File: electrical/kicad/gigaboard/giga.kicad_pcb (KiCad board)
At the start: 2 copper layers, 88.3 x 54 mm, 2 parts

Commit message: update(giga): pcb layout #01
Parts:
- removed ?: , clipboard:050be39d-fed9-491a-89e1-a26c1a1eb318
- added F1: F_Small, Fuse_TE5_Littlefuse-395Series, F.Cu at (120.0, 89.9)
- added REF**: PinHeader_1x04_P2.54mm_Vertical, Connector_PinHeader_2.54mm:PinHeader_1x04_P2.54mm_Vertical, F.Cu at (181.0, 58.1)
- added REF**: MKS_TMC2209, Motor_Driver:MKS_TMC2209, F.Cu at (151.0, 61.9)
- added REF**: JST_EH_B4B-EH-A_1x04_P2.50mm_Vertical, Connector_JST:JST_EH_B4B-EH-A_1x04_P2.50mm_Vertical, F.Cu at (207.0, 59.2)
- added REF**: TerminalBlock_Phoenix_MKDS-1,5-3-5.08_1x03_P5.08mm_Horizont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, TerminalBlock_Phoenix:TerminalBlock_Phoenix_MKDS-1,5-3-5.08_1x03_P5.08mm_Horizontal, F.Cu at (112.0, 91.0)
- added REF**: MKS_TMC2209, Motor_Driver:MKS_TMC2209, F.Cu at (170.7, 61.0)
- added REF**: MKS_TMC2209, Motor_Driver:MKS_TMC2209, F.Cu at (151.0, 83.0)
- added REF**: PinHeader_1x04_P2.54mm_Vertical, Connector_PinHeader_2.54mm:PinHeader_1x04_P2.54mm_Vertical, F.Cu at (140.0, 58.1)
- added REF**: PinHeader_2x10_P2.54mm_Vertical, Connector_PinHeader_2.54mm:PinHeader_2x10_P2.54mm_Vertical, F.Cu at (188.0, 54.3)
- added REF**: PinHeader_1x04_P2.54mm_Vertical, Connector_PinHeader_2.54mm:PinHeader_1x04_P2.54mm_Vertical, F.Cu at (140.0, 79.2)
- added REF**: JST_EH_B4B-EH-A_1x04_P2.50mm_Vertical, Connector_JST:JST_EH_B4B-EH-A_1x04_P2.50mm_Vertical, F.Cu at (189.5, 89.0)
- added REF**: JST_EH_B4B-EH-A_1x04_P2.50mm_Vertical, Connector_JST:JST_EH_B4B-EH-A_1x04_P2.50mm_Vertical, F.Cu at (201.5, 87.5)
- added REF**: MKS_TMC2209, Motor_Driver:MKS_TMC2209, F.Cu at (130.3, 82.9)
- added REF**: JST_EH_B4B-EH-A_1x04_P2.50mm_Vertical, Connector_JST:JST_EH_B4B-EH-A_1x04_P2.50mm_Vertical, F.Cu at (119.2, 62.2)
- added REF**: JST_EH_B4B-EH-A_1x04_P2.50mm_Vertical, Connector_JST:JST_EH_B4B-EH-A_1x04_P2.50mm_Vertical, F.Cu at (189.5, 94.0)
- added REF**: PinHeader_1x04_P2.54mm_Vertical, Connector_PinHeader_2.54mm:PinHeader_1x04_P2.54mm_Vertical, F.Cu at (160.7, 58.1)
- added REF**: MKS_TMC2209, Motor_Driver:MKS_TMC2209, F.Cu at (170.8, 82.0)
- added REF**: PinHeader_1x04_P2.54mm_Vertical, Connector_PinHeader_2.54mm:PinHeader_1x04_P2.54mm_Vertical, F.Cu at (160.7, 79.3)
- added REF**: JST_EH_B4B-EH-A_1x04_P2.50mm_Vertical, Connector_JST:JST_EH_B4B-EH-A_1x04_P2.50mm_Vertical, F.Cu at (206.9, 73.5)
- added REF**: JST_EH_B4B-EH-A_1x04_P2.50mm_Vertical, Connector_JST:JST_EH_B4B-EH-A_1x04_P2.50mm_Vertical, F.Cu at (206.9, 87.5)
- added REF**: JST_EH_B4B-EH-A_1x04_P2.50mm_Vertical, Connector_JST:JST_EH_B4B-EH-A_1x04_P2.50mm_Vertical, F.Cu at (201.5, 73.5)
- added REF**: MKS_TMC2209, Motor_Driver:MKS_TMC2209, F.Cu at (130.3, 61.9)
- added REF**: JST_EH_B4B-EH-A_1x04_P2.50mm_Vertical, Connector_JST:JST_EH_B4B-EH-A_1x04_P2.50mm_Vertical, F.Cu at (201.6, 59.2)
- added REF**: PinHeader_1x04_P2.54mm_Vertical, Connector_PinHeader_2.54mm:PinHeader_1x04_P2.54mm_Vertical, F.Cu at (167.2, 94.5)
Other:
- board size 88.3 x 54 mm -> 106.5 x 56 mm

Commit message: update(giga): pcb layout #02
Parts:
- removed REF** (x6): PinHeader_1x04_P2.54mm_Vertical, Connector_PinHeader_2.54mm:PinHeader_1x04_P2.54mm_Vertical
- removed REF** (x6): MKS_TMC2209, Motor_Driver:MKS_TMC2209
- removed REF** (x9): JST_EH_B4B-EH-A_1x04_P2.50mm_Vertical, Connector_JST:JST_EH_B4B-EH-A_1x04_P2.50mm_Vertical
- removed REF**: TerminalBlock_Phoenix_MKDS-1,5-3-5.08_1x03_P5.08mm_Horizont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, TerminalBlock_Phoenix:TerminalBlock_Phoenix_MKDS-1,5-3-5.08_1x03_P5.08mm_Horizontal
- removed REF**: PinHeader_2x10_P2.54mm_Vertical, Connector_PinHeader_2.54mm:PinHeader_2x10_P2.54mm_Vertical
- added C1: 100uF, Capacitor_SMD:CP_Elec_6.3x7.7, F.Cu at (107.4, 48.3)
- added C2: 100uF, Capacitor_SMD:CP_Elec_6.3x7.7, F.Cu at (107.4, 68.6)
- added C3: 100uF, Capacitor_SMD:CP_Elec_6.3x7.7, F.Cu at (127.8, 48.3)
- added C4: 100uF, Capacitor_SMD:CP_Elec_6.3x7.7, F.Cu at (127.8, 68.6)
- added C5: 100uF, Capacitor_SMD:CP_Elec_6.3x7.7, F.Cu at (148.1, 48.3)
- added C6: 100uF, Capacitor_SMD:CP_Elec_6.3x7.7, F.Cu at (148.1, 68.6)
- added D1: D, Diode_THT:D_DO-35_SOD27_P7.62mm_Horizontal, F.Cu at (97.8, 81.8)
- added J1: Conn_02x03_Counter_Clockwise, Connector_PinHeader_2.54mm:PinHeader_2x03_P2.54mm_Vertical, F.Cu at (104.9, 59.7)
- added J10: Conn_01x04, Connector_PinHeader_2.54mm:PinHeader_1x04_P2.54mm_Vertical, F.Cu at (137.9, 68.6)
- added J11: Conn_01x04, Connector_PinHeader_2.54mm:PinHeader_1x04_P2.54mm_Vertical, F.Cu at (158.8, 48.3)
- added J12: Conn_01x04, Connector_PinHeader_2.54mm:PinHeader_1x04_P2.54mm_Vertical, F.Cu at (158.8, 75.0)
- added J13: Conn_01x04, Connector_PinHeader_2.54mm:PinHeader_1x04_P2.54mm_Vertical, F.Cu at (176.5, 40.6)
- added J14: Conn_01x04, Connector_PinHeader_2.54mm:PinHeader_1x04_P2.54mm_Vertical, F.Cu at (176.5, 53.3)
- added J15: Conn_01x04, Connector_PinHeader_2.54mm:PinHeader_1x04_P2.54mm_Vertical, F.Cu at (176.5, 66.0)
- added J16: Conn_01x04, Connector_PinHeader_2.54mm:PinHeader_1x04_P2.54mm_Vertical, F.Cu at (180.3, 40.6)
- added J17: Conn_01x04, Connector_PinHeader_2.54mm:PinHeader_1x04_P2.54mm_Vertical, F.Cu at (180.3, 53.3)
- added J18: Conn_01x04, Connector_PinHeader_2.54mm:PinHeader_1x04_P2.54mm_Vertical, F.Cu at (180.3, 66.0)
- added J19: Conn_01x04, Connector_PinHeader_2.54mm:PinHeader_1x04_P2.54mm_Vertical, F.Cu at (96.5, 43.2)
- added J2: Conn_02x04_Counter_Clockwise, Connector_PinHeader_2.54mm:PinHeader_2x03_P2.54mm_Vertical, F.Cu at (104.9, 80.0)
- added J20: Conn_01x04, Connector_PinHeader_2.54mm:PinHeader_1x04_P2.54mm_Vertical, F.Cu at (162.6, 75.0)
- added J21: Conn_01x04, Connector_PinHeader_2.54mm:PinHeader_1x04_P2.54mm_Vertical, F.Cu at (166.4, 75.0)
- added J22: Screw_Terminal_01x03, Connector_Phoenix_MSTB:PhoenixContact_MSTBA_2,5_3-G-5,08_1x03_P5.08mm_Horizontal, F.Cu at (90.1, 60.7)
- added J23: Conn_02x12_Counter_Clockwise, Connector_PinHeader_2.54mm:PinHeader_2x12_P2.54mm_Vertical, F.Cu at (163.8, 43.2)
- added J3: Conn_02x04_Counter_Clockwise, Connector_PinHeader_2.54mm:PinHeader_2x03_P2.54mm_Vertical, F.Cu at (125.2, 59.7)
- added J4: Conn_02x04_Counter_Clockwise, Connector_PinHeader_2.54mm:PinHeader_2x03_P2.54mm_Vertical, F.Cu at (125.2, 80.0)
- added J5: Conn_02x04_Counter_Clockwise, Connector_PinHeader_2.54mm:PinHeader_2x03_P2.54mm_Vertical, F.Cu at (145.5, 59.7)
- added J6: Conn_02x04_Counter_Clockwise, Connector_PinHeader_2.54mm:PinHeader_2x03_P2.54mm_Vertical, F.Cu at (145.5, 80.0)
- added J7: Conn_01x04, Connector_PinHeader_2.54mm:PinHeader_1x04_P2.54mm_Vertical, F.Cu at (117.6, 48.3)
- added J8: Conn_01x04, Connector_PinHeader_2.54mm:PinHeader_1x04_P2.54mm_Vertical, F.Cu at (117.6, 68.6)
- added J9: Conn_01x04, Connector_PinHeader_2.54mm:PinHeader_1x04_P2.54mm_Vertical, F.Cu at (137.9, 48.3)
- added R1: 100k, Resistor_SMD:R_1206_3216Metric_Pad1.30x1.75mm_HandSolder, F.Cu at (104.9, 53.3)
- added R10: 10k, Resistor_SMD:R_1206_3216Metric_Pad1.30x1.75mm_HandSolder, F.Cu at (130.3, 73.7)
- added R11: 10k, Resistor_SMD:R_1206_3216Metric_Pad1.30x1.75mm_HandSolder, F.Cu at (150.6, 53.3)
- added R12: 10k, Resistor_SMD:R_1206_3216Metric_Pad1.30x1.75mm_HandSolder, F.Cu at (150.6, 73.7)
- added R2: 100k, Resistor_SMD:R_1206_3216Metric_Pad1.30x1.75mm_HandSolder, F.Cu at (104.9, 73.7)
- added R3: 100k, Resistor_SMD:R_1206_3216Metric_Pad1.30x1.75mm_HandSolder, F.Cu at (125.2, 53.3)
- added R4: 100k, Resistor_SMD:R_1206_3216Metric_Pad1.30x1.75mm_HandSolder, F.Cu at (125.2, 73.7)
- added R5: 100k, Resistor_SMD:R_1206_3216Metric_Pad1.30x1.75mm_HandSolder, F.Cu at (145.5, 53.3)
- added R6: 100k, Resistor_SMD:R_1206_3216Metric_Pad1.30x1.75mm_HandSolder, F.Cu at (145.5, 73.7)
- added R7: 10k, Resistor_SMD:R_1206_3216Metric_Pad1.30x1.75mm_HandSolder, F.Cu at (110.0, 53.3)
- added R8: 10k, Resistor_SMD:R_1206_3216Metric_Pad1.30x1.75mm_HandSolder, F.Cu at (110.0, 73.7)
- added R9: 10k, Resistor_SMD:R_1206_3216Metric_Pad1.30x1.75mm_HandSolder, F.Cu at (130.3, 53.3)
- added U1: TMC2209, Motor_Driver:MKS_TMC2209, F.Cu at (107.4, 52.1)
- added U2: TMC2209, Motor_Driver:MKS_TMC2209, F.Cu at (107.4, 72.4)
- added U3: TMC2209, Motor_Driver:MKS_TMC2209, F.Cu at (127.8, 52.1)
- added U4: TMC2209, Motor_Driver:MKS_TMC2209, F.Cu at (127.8, 72.4)
- added U5: TMC2209, Motor_Driver:MKS_TMC2209, F.Cu at (148.1, 52.1)
- added U6: TMC2209, Motor_Driver:MKS_TMC2209, F.Cu at (148.1, 72.4)
- F1: footprint Fuse_TE5_Littlefuse-395Series -> Fuse:Fuseholder_Blade_Mini_Keystone_3568
- moved F1 39.3 mm to (82.8, 77.4), turned to 0 degrees
- moved A1 26.3 mm to (76.2, 88.9)
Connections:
- A1 pad AREF: /BAT_MAX -> /+3.3V
- A1 pad D22: /TCA_RST -> /ESTOP
- A1 pad D54: (no net) -> unconnected-(A1-PadD54)
- A1 pad D55: (no net) -> unconnected-(A1-PadD55)
- A1 pad D56: (no net) -> unconnected-(A1-PadD56)
- A1 pad D57: (no net) -> unconnected-(A1-PadD57)
- A1 pad D58: (no net) -> unconnected-(A1-PadD58)
- A1 pad D59: (no net) -> unconnected-(A1-PadD59)
- A1 pad D60: (no net) -> unconnected-(A1-PadD60)
- A1 pad D61: (no net) -> unconnected-(A1-PadD61)
- A1 pad D62: (no net) -> unconnected-(A1-PadD62)
- A1 pad D63: (no net) -> unconnected-(A1-PadD63)
- A1 pad D64: (no net) -> unconnected-(A1-PadD64)
- A1 pad D65: (no net) -> unconnected-(A1-PadD65)
- A1 pad D66: (no net) -> unconnected-(A1-PadD66)
- A1 pad D67: (no net) -> unconnected-(A1-PadD67)
- A1 pad D68: (no net) -> unconnected-(A1-PadD68)
- A1 pad D69: (no net) -> unconnected-(A1-PadD69)
- A1 pad D70: (no net) -> unconnected-(A1-PadD70)
- A1 pad D71: (no net) -> unconnected-(A1-PadD71)
- A1 pad D72: (no net) -> unconnected-(A1-PadD72)
- A1 pad D73: (no net) -> unconnected-(A1-PadD73)
- A1 pad D74: (no net) -> unconnected-(A1-PadD74)
- A1 pad D75: (no net) -> unconnected-(A1-PadD75)
- F1 pad 1: (no net) -> /VM
- F1 pad 2: (no net) -> Net-(D1-K)
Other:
- board size 106.5 x 56 mm -> 108 x 66 mm

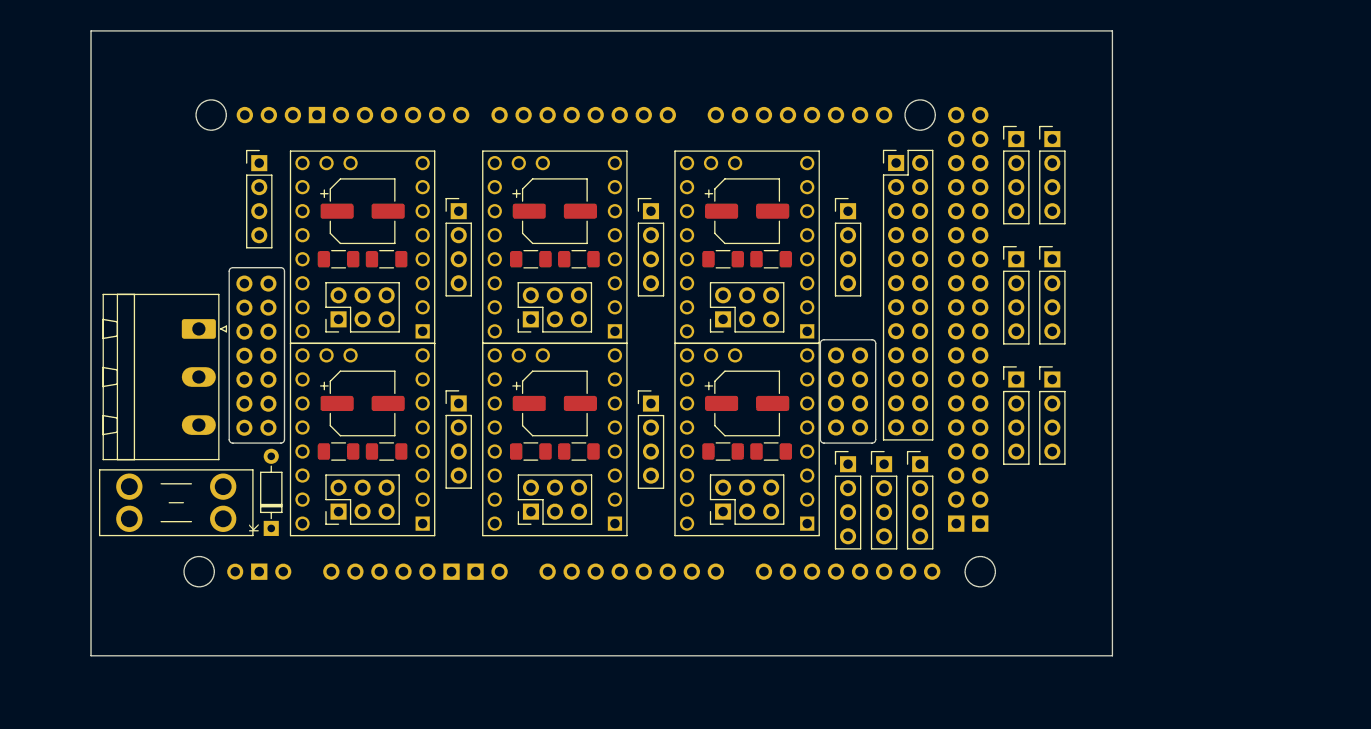
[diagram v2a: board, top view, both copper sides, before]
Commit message: update(giga): pcb wiring complete (DRC passed)
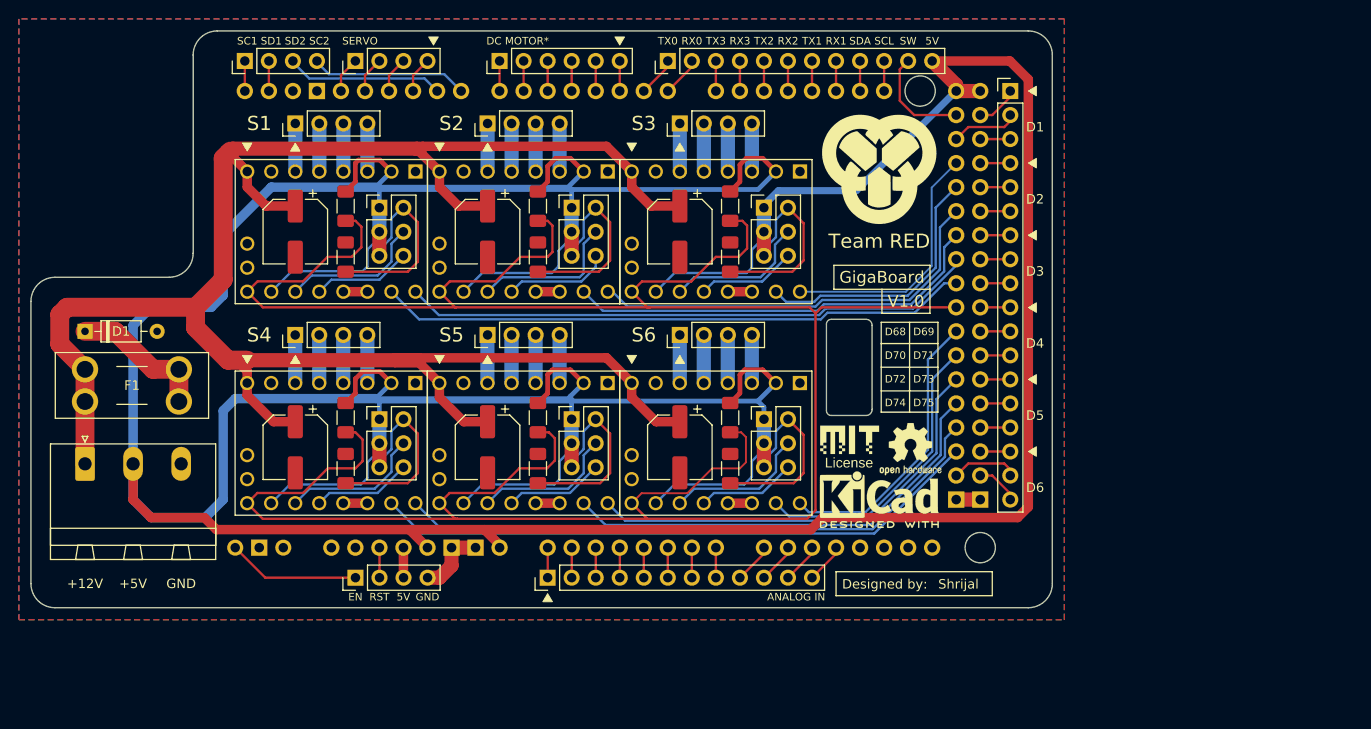
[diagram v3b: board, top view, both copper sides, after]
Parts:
- removed J21: Conn_01x04, Connector_PinHeader_2.54mm:PinHeader_1x04_P2.54mm_Vertical
- removed J22: Screw_Terminal_01x03, Connector_Phoenix_MSTB:PhoenixContact_MSTBA_2,5_3-G-5,08_1x03_P5.08mm_Horizontal
- removed J23: Conn_02x12_Counter_Clockwise, Connector_PinHeader_2.54mm:PinHeader_2x12_P2.54mm_Vertical
- added G***: LOGO, LOGO, F.Cu at (158.9, 73.2)
- added G***: LOGO, LOGO, F.Cu at (161.9, 43.8)
- added REF**: OSHW-Logo2_7.3x6mm_SilkScreen, Symbol:OSHW-Logo2_7.3x6mm_SilkScreen, F.Cu at (165.4, 73.4)
- added REF**: KiCad-Logo2_5mm_SilkScreen, Symbol:KiCad-Logo2_5mm_SilkScreen, F.Cu at (162.1, 78.7)
- J13: value Conn_01x04 -> Conn_01x06; footprint Connector_PinHeader_2.54mm:PinHeader_1x04_P2.54mm_Vertical -> Connector_PinHeader_2.54mm:PinHeader_1x06_P2.54mm_Vertical
- J14: value Conn_01x04 -> Conn_01x18; footprint Connector_PinHeader_2.54mm:PinHeader_1x04_P2.54mm_Vertical -> Connector_PinHeader_2.54mm:PinHeader_1x18_P2.54mm_Vertical
- J16, J18: value Conn_01x04 -> Conn_01x12; footprint Connector_PinHeader_2.54mm:PinHeader_1x04_P2.54mm_Vertical -> Connector_PinHeader_2.54mm:PinHeader_1x12_P2.54mm_Vertical
- J20: value Conn_01x04 -> Screw_Terminal_01x03; footprint Connector_PinHeader_2.54mm:PinHeader_1x04_P2.54mm_Vertical -> Connector_Phoenix_MSTB:PhoenixContact_MSTBA_2,5_3-G-5,08_1x03_P5.08mm_Horizontal
- moved J17 87.9 mm to (95.0, 32.4), turned to 90 degrees
- moved J20 84.5 mm to (78.1, 75.0)
- moved J15 77.5 mm to (106.7, 32.4), turned to 90 degrees
- moved J16 70.7 mm to (127.0, 87.0), turned to 90 degrees
- moved J13 55.2 mm to (121.9, 32.4), turned to 90 degrees
- moved J18 52.8 mm to (139.7, 32.4), turned to 90 degrees
- moved J19 45.0 mm to (106.7, 87.0), turned to 90 degrees
- moved J2 40.5 mm to (129.5, 47.9), turned to 0 degrees
- moved J11 40.3 mm to (120.7, 61.3), turned to 90 degrees
- moved J10 38.3 mm to (100.3, 61.3), turned to 90 degrees
- moved C5 37.1 mm to (120.7, 73.2), turned to -90 degrees
- moved U5 31.4 mm to (124.5, 72.8), turned to -90 degrees
- moved R8 30.5 mm to (126.0, 47.7), turned to -90 degrees
- moved R11 29.8 mm to (126.0, 70.1), turned to -90 degrees
- moved J8 29.7 mm to (120.7, 39.0), turned to 90 degrees
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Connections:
- A1 pad AREF: /+3.3V -> unconnected-(A1-PadAREF)
- A1 pad D26: /DC2_DIR -> /ST3_DIR
- A1 pad D27: /DC2_CHA -> /DC2_DIR
- A1 pad D28: /DC2_CHB -> /ST3_STP
- A1 pad D29: /DC3_DIR -> /DC2_CHA
- A1 pad D30: /DC3_CHA -> /ST2_DIR
- A1 pad D31: /DC3_CHB -> /DC2_CHB
- A1 pad D32: /DC4_DIR -> /ST2_STP
- A1 pad D33: /DC4_CHA -> /DC3_DIR
- A1 pad D34: /DC4_CHB -> /ST1_DIR
- A1 pad D35: /DC5_DIR -> /DC3_CHA
- A1 pad D36: /DC5_CHA -> /ST1_STP
- A1 pad D37: /DC5_CHB -> /DC3_CHB
- A1 pad D38: /DC6_DIR -> /STP_ENA
- A1 pad D39: /DC6_CHA -> /DC4_DIR
- A1 pad D40: /DC6_CHB -> /ST6_DIR
- A1 pad D41: /STP_ENA -> /DC4_CHA
- A1 pad D42: /ST1_STP -> /ST6_STP
- A1 pad D43: /ST1_DIR -> /DC4_CHB
- A1 pad D44: /ST2_STP -> /ST5_DIR
- A1 pad D45: /ST2_DIR -> /DC5_DIR
- A1 pad D46: /ST3_STP -> /ST5_STP
- A1 pad D47: /ST3_DIR -> /DC5_CHA
- A1 pad D48: /ST4_STP -> /ST4_DIR
- A1 pad D49: /ST4_DIR -> /DC5_CHB
- A1 pad D50: /ST5_STP -> /ST4_STP
- A1 pad D51: /ST5_DIR -> /DC6_DIR
- A1 pad D52: /ST6_STP -> /DC6_CHA
- A1 pad D53: /ST6_DIR -> /DC6_CHB
- J13 pad 1: /DC1_PWM -> /DC6_PWM
- J13 pad 2: /DC1_DIR -> /DC5_PWM
- J13 pad 3: /DC1_CHA -> /DC4_PWM
- J13 pad 4: /DC1_CHB -> /DC3_PWM
- J14 pad 1: /DC2_PWM -> /DC1_DIR
- J14 pad 2: /DC2_DIR -> /DC1_CHA
- J14 pad 3: /DC2_CHA -> /DC1_CHB
- J14 pad 4: /DC2_CHB -> /DC2_DIR
- J15 pad 1: /DC3_PWM -> /SV4_PWM
- J15 pad 2: /DC3_DIR -> /SV3_PWM
- J15 pad 3: /DC3_CHA -> /SV2_PWM
- J15 pad 4: /DC3_CHB -> /SV1_PWM
- J16 pad 1: /DC4_PWM -> /BAT1_S1
- J16 pad 2: /DC4_DIR -> /BAT1_S2
- J16 pad 3: /DC4_CHA -> /BAT1_S3
- J16 pad 4: /DC4_CHB -> /BAT1_S4
- J17 pad 1: /DC5_PWM -> /INA_SDA
- J17 pad 2: /DC5_DIR -> /INA_SCL
- J17 pad 3: /DC5_CHA -> /SDA
- J17 pad 4: /DC5_CHB -> /SCL
- J18 pad 1: /DC6_PWM -> /Pi5_RX
- J18 pad 2: /DC6_DIR -> /Pi5_TX
- J18 pad 3: /DC6_CHA -> /TX3
- J18 pad 4: /DC6_CHB -> /RX3
- J19 pad 1: (no net) -> /GIGA_EN
- J19 pad 2: (no net) -> /GIGA_RST
- J19 pad 3: (no net) -> /+3.3V
- J19 pad 4: (no net) -> /GND
- J20 pad 1: /BAT1_S1 -> /VM
- J20 pad 2: /BAT1_S2 -> /+5V
- J20 pad 3: /BAT1_S3 -> /GND
- U1 pad 11: unconnected-(U1-PDN-Pad11) -> Net-(U1-PDN)
- U1 pad 12: unconnected-(U1-UART-Pad12) -> Net-(U1-PDN)
- U2 pad 11: unconnected-(U2-PDN-Pad11) -> Net-(U2-PDN)
- U2 pad 12: unconnected-(U2-UART-Pad12) -> Net-(U2-PDN)
- U3 pad 11: unconnected-(U3-PDN-Pad11) -> Net-(U3-PDN)
- U3 pad 12: unconnected-(U3-UART-Pad12) -> Net-(U3-PDN)
- U4 pad 11: unconnected-(U4-PDN-Pad11) -> Net-(U4-PDN)
- U4 pad 12: unconnected-(U4-UART-Pad12) -> Net-(U4-PDN)
- U5 pad 11: unconnected-(U5-PDN-Pad11) -> Net-(U5-PDN)
- U5 pad 12: unconnected-(U5-UART-Pad12) -> Net-(U5-PDN)
- U6 pad 11: unconnected-(U6-PDN-Pad11) -> Net-(U6-PDN)
- U6 pad 12: unconnected-(U6-UART-Pad12) -> Net-(U6-PDN)
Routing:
- net /+5V: track 0.00 -> 470.6 mm
- net /STP_ENA: track 0.00 -> 278.4 mm
- net /VM: track 0.00 -> 205.0 mm
- net /ST4_STP: track 0.00 -> 64.6 mm
- net /ST4_DIR: track 0.00 -> 63.9 mm
- net /ST1_STP: track 0.00 -> 62.5 mm
- net /ST1_DIR: track 0.00 -> 61.0 mm
- net /ST5_STP: track 0.00 -> 47.9 mm
- net /ST5_DIR: track 0.00 -> 47.1 mm
- net /ST2_STP: track 0.00 -> 45.0 mm
- net /ST2_DIR: track 0.00 -> 44.5 mm
- net Net-(J3-Pin_2): track 0.00 -> 34.4 mm
- net Net-(J1-Pin_2): track 0.00 -> 34.3 mm
- net Net-(J5-Pin_2): track 0.00 -> 34.3 mm
- net Net-(J6-Pin_2): track 0.00 -> 34.2 mm
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- added copper zone on B.Cu, net /GND
- added copper zone on F.Cu, net /GND
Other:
- board size 108 x 66 mm -> 108 x 61 mm
- board text added: "+12V"
- board text added: "+5V"
- board text added: "5V"
- board text added: "ANALOG IN"
- board text added: "D1"
- board text added: "D2"
- board text added: "D3"
- board text added: "D4"
- board text added: "D5"
- board text added: "D6"
- board text added: "D68"
- board text added: "D69"
- board text added: "D70"
- board text added: "D71"
- board text added: "D72"
- board text added: "D73"
- board text added: "D74"
- board text added: "D75"
- board text added: "DC MOTOR*"
- board text added: "Designed by:"
- board text added: "EN"
- board text added: "GND"
- board text added: "GigaBoard"
- board text added: "RST"
- board text added: "RX0"
- board text added: "RX1"
- board text added: "RX2"
- board text added: "RX3"
- board text added: "S1"
- board text added: "S2"
- board text added: "S3"
- board text added: "S4"
- board text added: "S5"
- board text added: "S6"
- board text added: "SC1"
- board text added: "SC2"
- board text added: "SCL"
- board text added: "SD1"
- board text added: "SD2"
- board text added: "SDA"
- board text added: "SERVO"
- board text added: "SW"
- board text added: "Shrijal"
- board text added: "TX0"
- board text added: "TX1"
- board text added: "TX2"
- board text added: "TX3"
- board text added: "Team RED"
- board text added: "V1.0"
